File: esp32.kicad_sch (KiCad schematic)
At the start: 52 parts, among them J2 Conn_01x05, SW1 Reset, SW2 BOOT, U15 MPR121QR2, U8 ESP32-S3R8, U9 W25Q128JVSIQ, Y1 40MHz

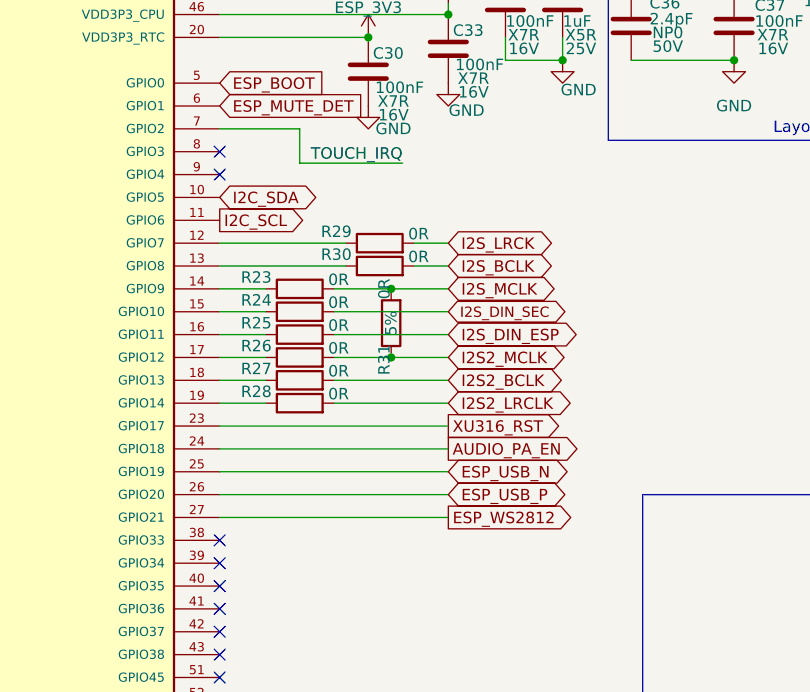
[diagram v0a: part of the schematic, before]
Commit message: v2.1: octilinear re-route of added tracks, bundled JTAG, TI-style buck layout, v2.1 silkscreen
All tracks added in v2-fix re-routed at 0/45/90 deg with no mid-trace splits; branches only at pads or vias. JTAG runs as one parallel bundle (J4 moved to the top side). Buck converter re-laid with power polygons. XU316_RST moved to GPIO21, LED data to GPIO4, X1D11 MCLK left unconnected; MiciMike.yaml updated to match. Silkscreen and title blocks now say v2.1. KiCad 9 DRC with schematic parity shows only the items already on the v2 board. See CHANGES-v2fix.md.

Co-Authored-By: Claude Opus 5.5 <noreply@anthropic.com>
Claude-Session: https://claude.ai/code/session_01DBYfebaHp5UuC2Xws8yAJw
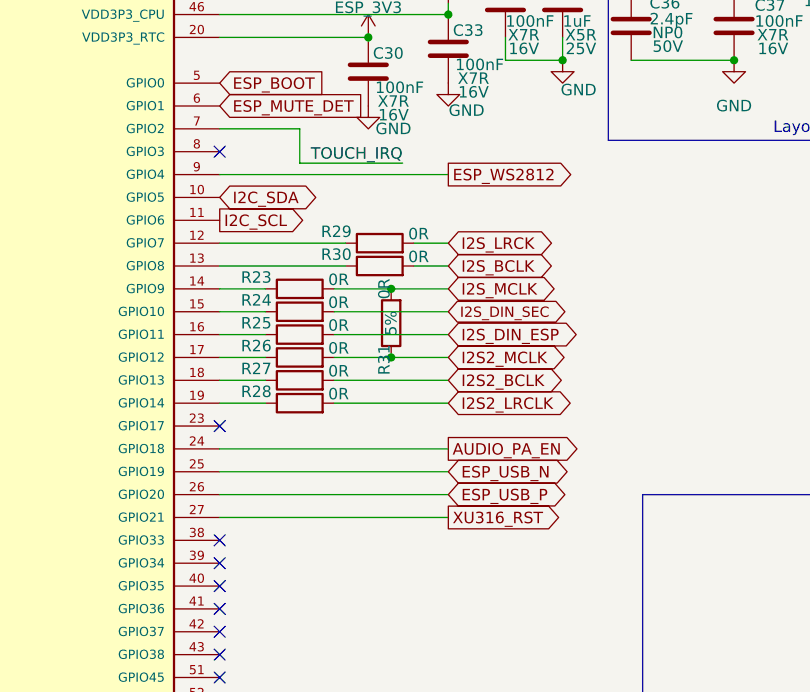
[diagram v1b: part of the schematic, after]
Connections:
- net ESP_WS2812: now also U8.9 (GPIO4); no longer U8.27 (GPIO21)
- net XU316_RST: now also U8.27 (GPIO21); no longer U8.23 (GPIO17)
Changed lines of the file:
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@@
 	(title_block
 		(title "Drop in replacement PCB for Nest mini GEN2")
-		(rev "v1")
+		(rev "v2.1")
 		(company "by iMike78 (inpired by Onju voice and HA VPE)")
 	)
@@
 	)
 	(no_connect
-		(at 148.59 54.61)
+		(at 148.59 82.55)
 	)
 	(no_connect
@@
 	(wire
 		(pts
-			(xy 148.59 82.55) (xy 173.99 82.55)
+			(xy 148.59 54.61) (xy 173.99 54.61)
 		)
 		(stroke
@@
 		)
 	)
-	(global_label "XU316_RST"
+	(global_label "ESP_WS2812"
 		(shape output)
-		(at 173.99 82.55 0)
+		(at 173.99 54.61 0)
 		(fields_autoplaced yes)
 		(effects
@@
 		)
 		(property "Intersheetrefs" "${INTERSHEET_REFS}"
-			(at 187.5584 82.55 0)
+			(at 187.5584 54.61 0)
 			(effects
 				(font
@@
 		)
 	)
-	(global_label "ESP_WS2812"
+	(global_label "XU316_RST"
 		(shape output)
 		(at 173.99 92.71 0)
